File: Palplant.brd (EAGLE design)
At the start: 79.9 x 35 mm, 28 parts, among them IC2 MCP73831/OT, U2 ESP-12E/F

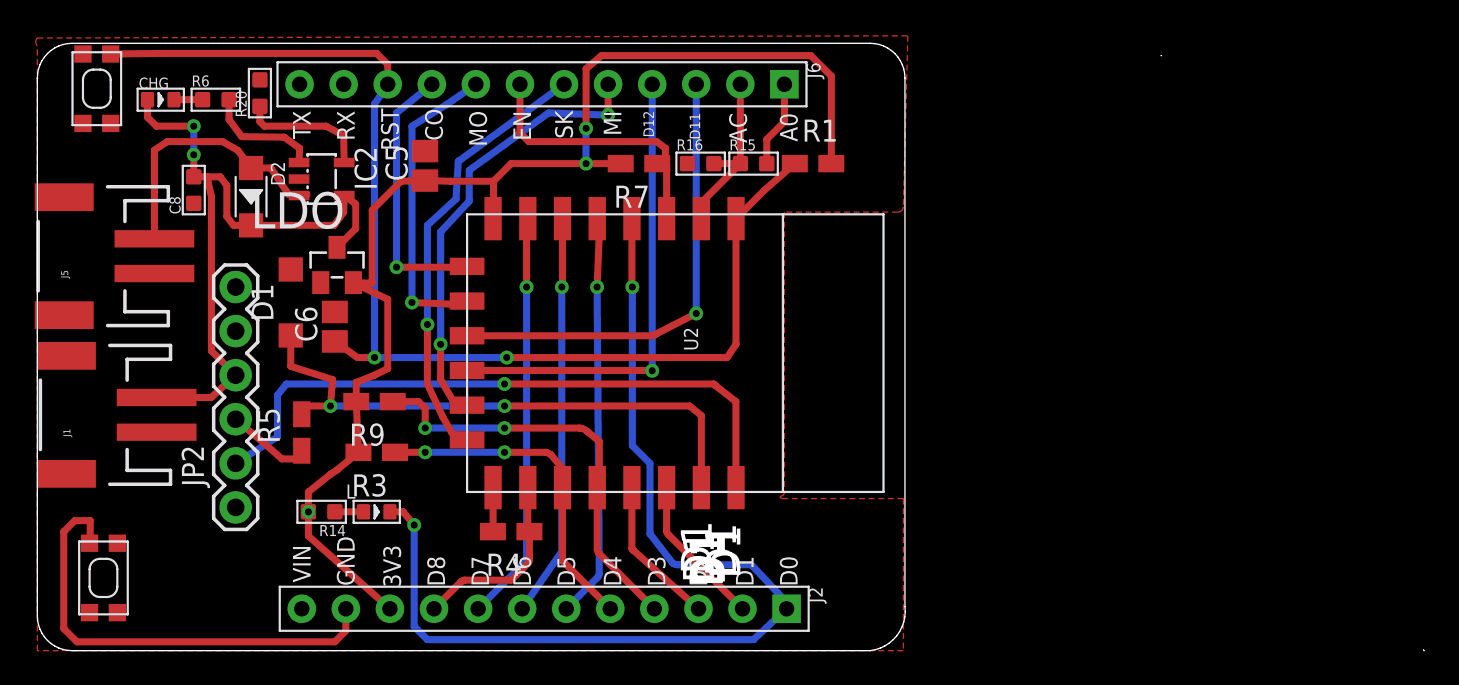
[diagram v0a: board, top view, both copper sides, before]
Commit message: The resistor now use the same reference and package
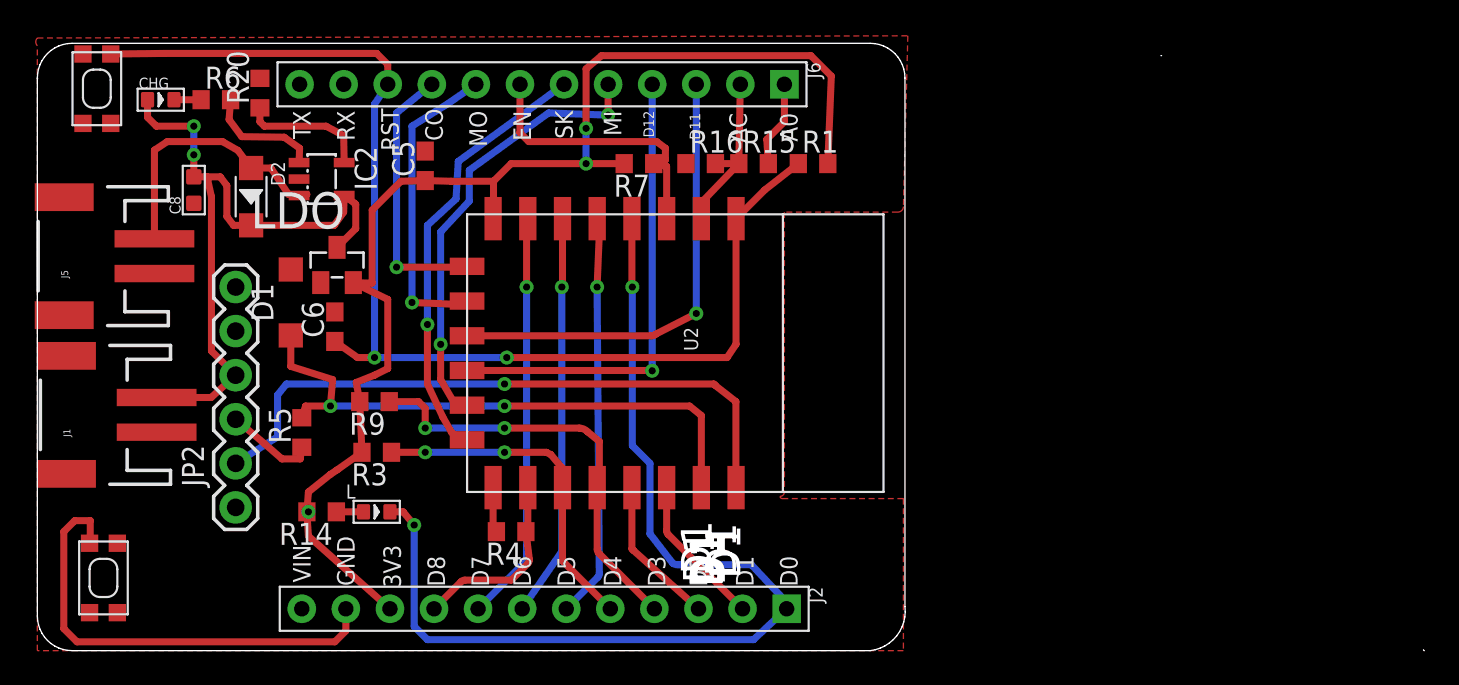
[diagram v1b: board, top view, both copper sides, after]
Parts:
- C5, C6: device adafruit:C0805 -> rcl:C0603
- R1, R3, R4, R5, R7, R9: device resistor:R0805W -> rcl:R0603
- R14, R15, R16, R20, R6: device Discrete:R0603 -> rcl:R0603
